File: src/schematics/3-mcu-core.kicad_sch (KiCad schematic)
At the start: 53 parts, among them Q1 MMBT3904, U301 PIC32CX1025SG41100T-I/E5X

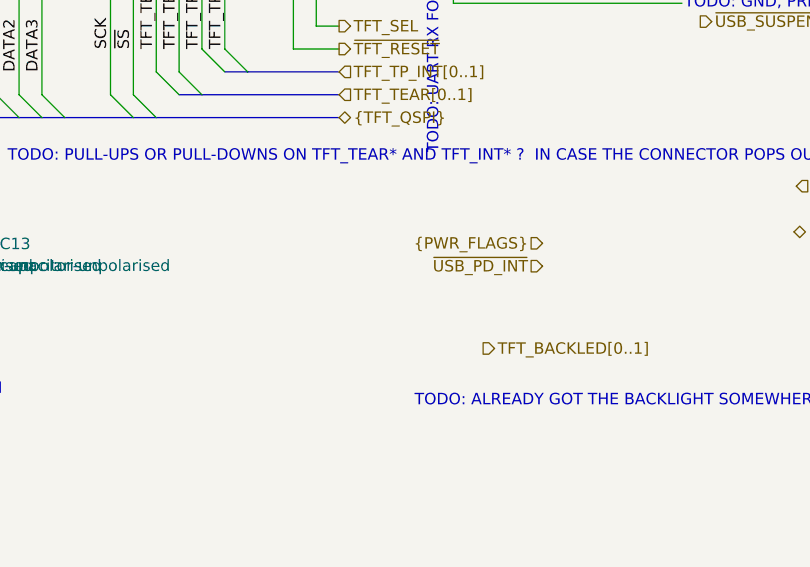
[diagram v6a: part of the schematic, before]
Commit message: Further elaboration of the USB / Power schematic.
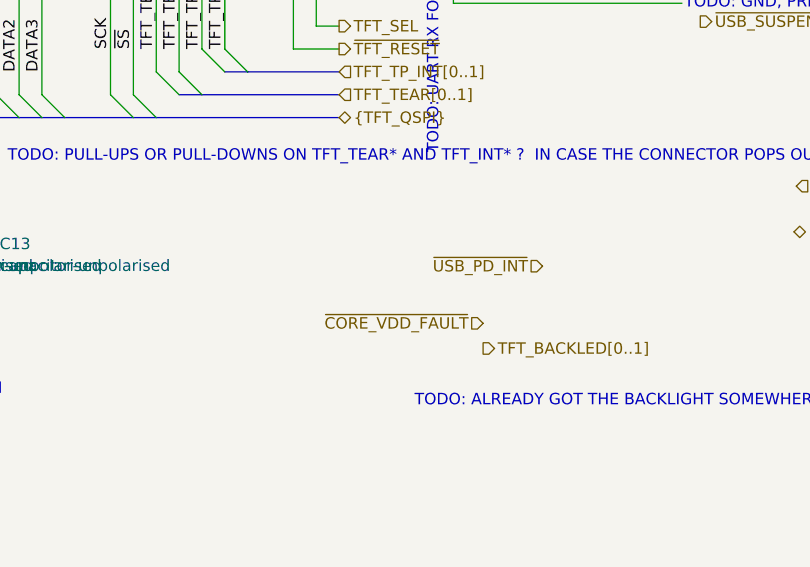
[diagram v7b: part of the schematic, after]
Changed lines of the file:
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@@
     (effects (font (size 1.27 1.27)) (justify left))
+  )
+  (hierarchical_label "~{CORE_VDD_FAULT}" (shape input) (at 203.962 251.46 180) (fields_autoplaced)
+    (effects (font (size 1.27 1.27)) (justify right))
   )
   (hierarchical_label "{SDCARD_DATA}" (shape bidirectional) (at 309.88 111.76 0) (fields_autoplaced)
@@
     (effects (font (size 1.27 1.27)) (justify left))
   )
-  (hierarchical_label "{PWR_FLAGS}" (shape input) (at 210.566 242.57 180) (fields_autoplaced)
-    (effects (font (size 1.27 1.27)) (justify right))
-  )
   (hierarchical_label "{IR_RCV}" (shape bidirectional) (at 238.506 241.3 0) (fields_autoplaced)

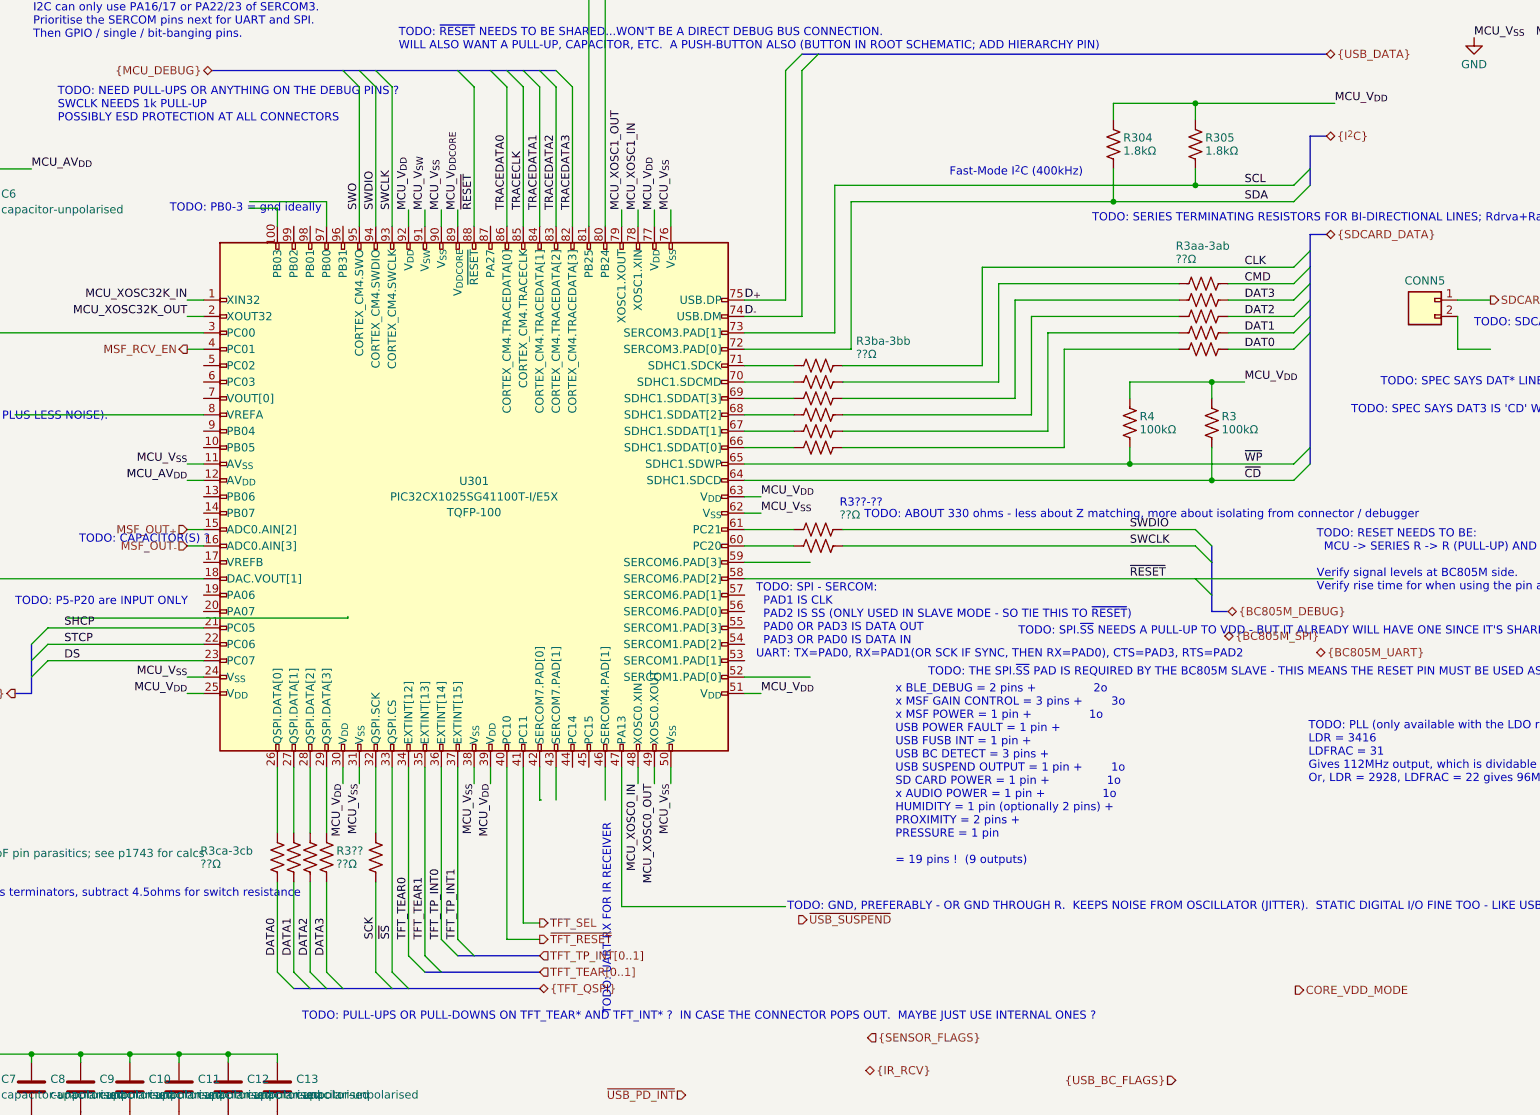
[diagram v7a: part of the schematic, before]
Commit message: Initial stab at a simulation for the buck regulator.  Started to flesh out the USB / power schematics.  More work required to figure out the large ripple on the buck regulator's input, which looks to be related to the ESL of the input capacitors.
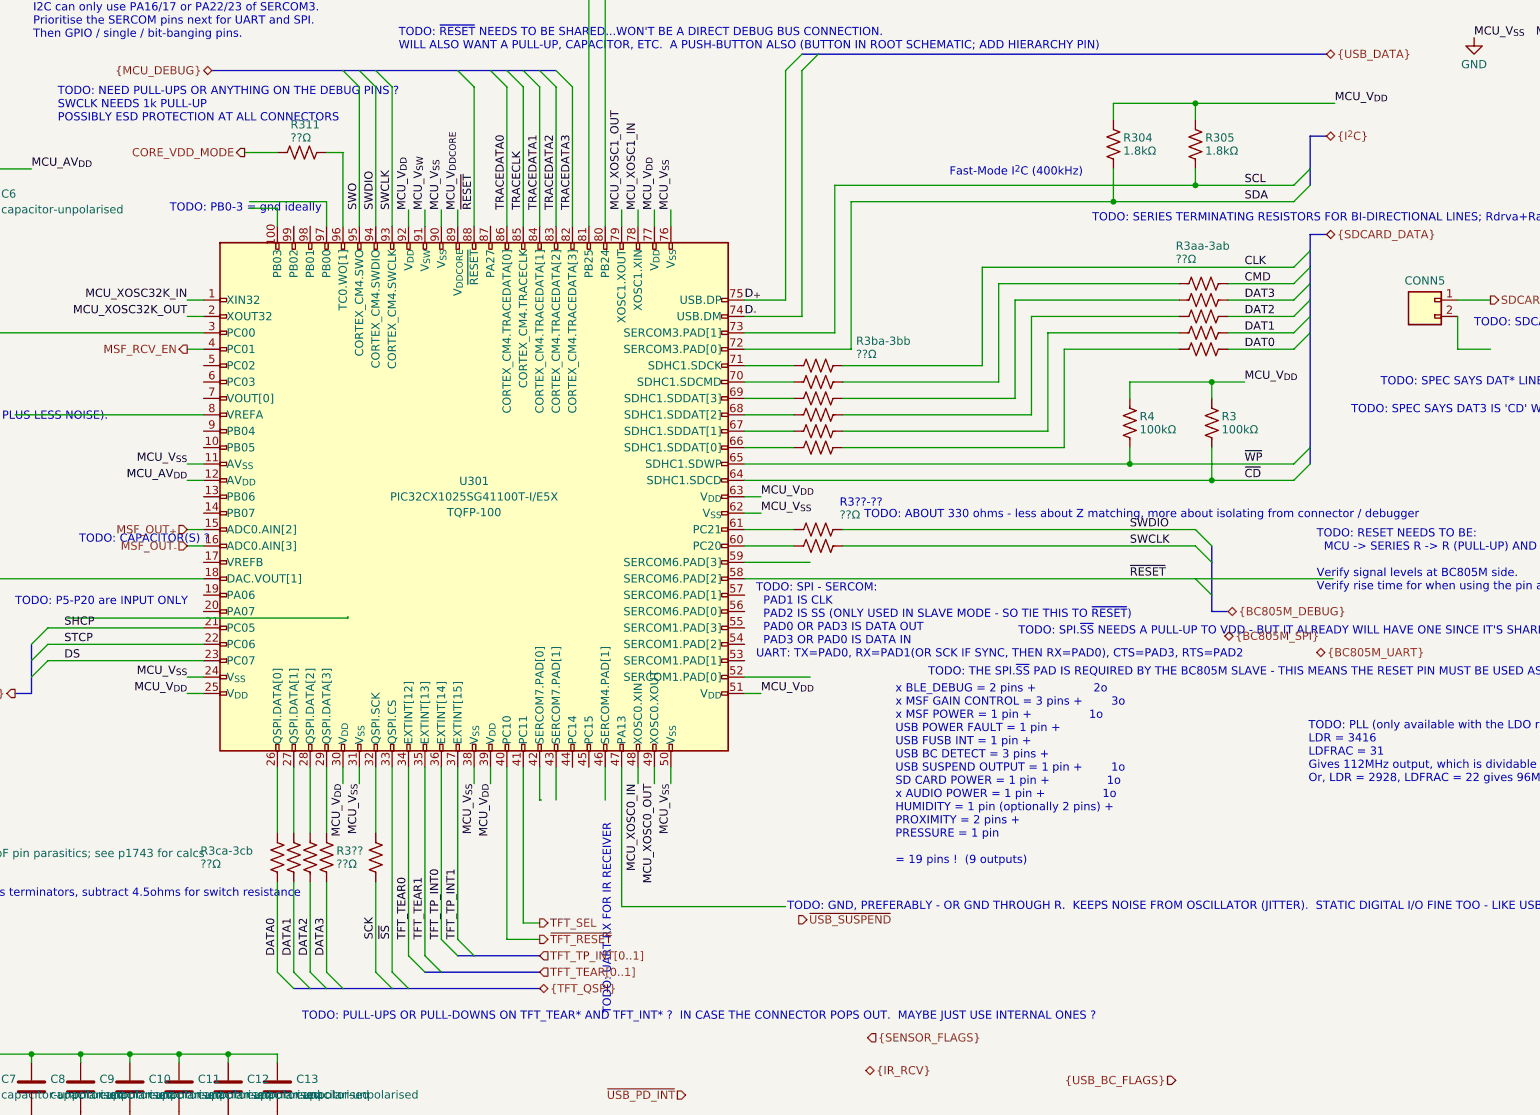
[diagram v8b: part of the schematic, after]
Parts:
- added R311: ??Ω, restall-generic-resistors:nominal-0402-1005, symbol restall-generic-resistors:resistor
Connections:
- net CORE_VDD_MODE: now also R311.1
- net at U301.96 (PB31): now also R311.2
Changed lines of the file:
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@@
     (stroke (width 0) (type default))
   )
+  (wire (pts (xy 142.24 99.06) (xy 147.32 99.06))
+    (stroke (width 0) (type default))
+  )
   (wire (pts (xy 226.06 86.36) (xy 226.06 121.92))
     (stroke (width 0) (type default))
@@
     (stroke (width 0) (type default))
   )
+  (wire (pts (xy 157.48 110.49) (xy 157.48 99.06))
+    (stroke (width 0) (type default))
+  )
   (wire (pts (xy 294.64 124.46) (xy 304.8 124.46))
     (stroke (width 0) (type default))
@@
     (stroke (width 0) (type default))
   )
+  (wire (pts (xy 154.94 99.06) (xy 157.48 99.06))
+    (stroke (width 0) (type default))
+  )
   (wire (pts (xy 219.71 162.56) (xy 229.87 162.56))
     (stroke (width 0) (type default))
@@
     (effects (font (size 1.27 1.27)) (justify right))
   )
-  (hierarchical_label "CORE_VDD_MODE" (shape output) (at 305.054 228.854 0) (fields_autoplaced)
-    (effects (font (size 1.27 1.27)) (justify left))
+  (hierarchical_label "CORE_VDD_MODE" (shape output) (at 142.24 99.06 180) (fields_autoplaced)
+    (effects (font (size 1.27 1.27)) (justify right))
   )
   (hierarchical_label "{MCU_DEBUG}" (shape bidirectional) (at 137.16 86.36 180) (fields_autoplaced)
@@
     )
   )
+  (symbol (lib_id "restall-generic-resistors:resistor") (at 151.13 99.06 90) (unit 1)
+    (in_bom yes) (on_board yes) (dnp no)
+    (property "Reference" "R311" (at 149.352 94.742 90)
+      (effects (font (size 1.27 1.27)) (justify right))
+    )
+    (property "Value" "??Ω" (at 149.352 96.774 90)
+      (effects (font (size 1.27 1.27)) (justify right))
+    )
+    (property "Footprint" "restall-generic-resistors:nominal-0402-1005" (at 151.384 98.044 90)
+      (effects (font (size 1.27 1.27)) (justify right) hide)
+    )
+    (property "Datasheet" "~" (at 151.13 99.06 0)
+      (effects (font (size 1.27 1.27)) (justify left) hide)
+    )
+    (property "Label" "??Ω±1% 0.0625W" (at 152.654 97.282 0)
+      (effects (font (size 1.27 1.27)) (justify left) hide)
+    )
+    (property "Tolerance" "±1%" (at 154.686 97.282 0)
+      (effects (font (size 1.27 1.27)) (justify left) hide)
+    )
+    (property "PowerRating" "0.0625W" (at 156.718 97.282 0)
+      (effects (font (size 1.27 1.27)) (justify left) hide)
+    )
+    (property "TemperatureCoefficient" "±100ppm" (at 158.75 97.282 0)
+      (effects (font (size 1.27 1.27)) (justify left) hide)
+    )
+    (property "Construction" "Thick Film" (at 160.782 97.282 0)
+      (effects (font (size 1.27 1.27)) (justify left) hide)
+    )
+    (property "Package" "0402" (at 162.814 97.282 0)
+      (effects (font (size 1.27 1.27)) (justify left) hide)
+    )
+    (property "Manufacturer" "" (at 151.13 99.06 0)
+      (effects (font (size 1.27 1.27)) (justify left) hide)
+    )
+    (property "ManufacturerPartNumber" "" (at 151.13 99.06 0)
+      (effects (font (size 1.27 1.27)) (justify left) hide)
+    )
+    (property "Manufacturer2" "" (at 151.13 99.06 0)
+      (effects (font (size 1.27 1.27)) (justify left) hide)
+    )
+    (property "Manufacturer2PartNumber" "" (at 151.13 99.06 0)
+      (effects (font (size 1.27 1.27)) (justify left) hide)
+    )
+    (pin "1")
+    (pin "2")
+    (instances
+      (project "msf-owl-clock"
+        (path "/56d623d3-22db-4d43-a9d9-e6bb4bb68946/cc278a5b-e802-444a-81ef-f38d11985404"
+          (reference "R311") (unit 1)
+        )
+      )
+    )
+  )
   (symbol (lib_id "restall-generic-resistors:resistor") (at 231.14 139.7 90) (unit 1)
     (in_bom yes) (on_board yes) (dnp no)
@@
     (pin "61")
     (pin "51")
-    (pin "96")
+    (pin "96" (alternate "TC0.WO[1]"))
     (pin "94" (alternate "CORTEX_CM4.SWDIO"))
     (pin "66" (alternate "SDHC1.SDDAT[0]"))
